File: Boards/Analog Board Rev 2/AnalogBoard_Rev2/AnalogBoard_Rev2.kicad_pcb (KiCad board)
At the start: 4 copper layers, 59.5 x 114.5 mm, 56 parts, among them J1 Conn_01x06_Male, J2 Conn_01x10_Male, J3 Conn_01x06_Male, J4 Conn_01x08_Male, SW1 SW_DIP_x04, U1 OPA2134, U12 NSL-32, U13 NSL-32, U2 OPA2134, U3 OPA2134, U4 OPA2134, U5 OPA2134, U6 NSL-32, U7 NSL-32, U8 NSL-32, U9 NSL-32

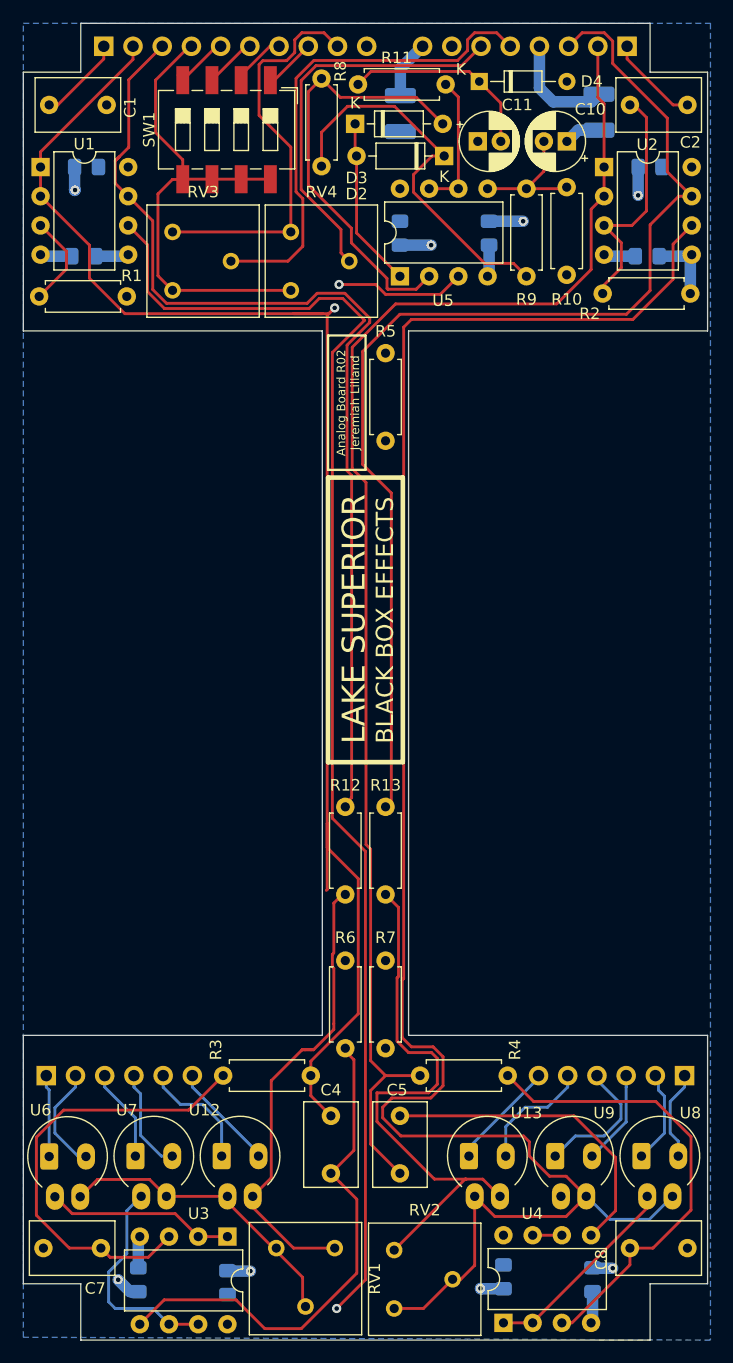
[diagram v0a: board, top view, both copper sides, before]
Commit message: reorg pt 1
Reorganizing, deleted a bunch of stuff. Probably will reorg some more
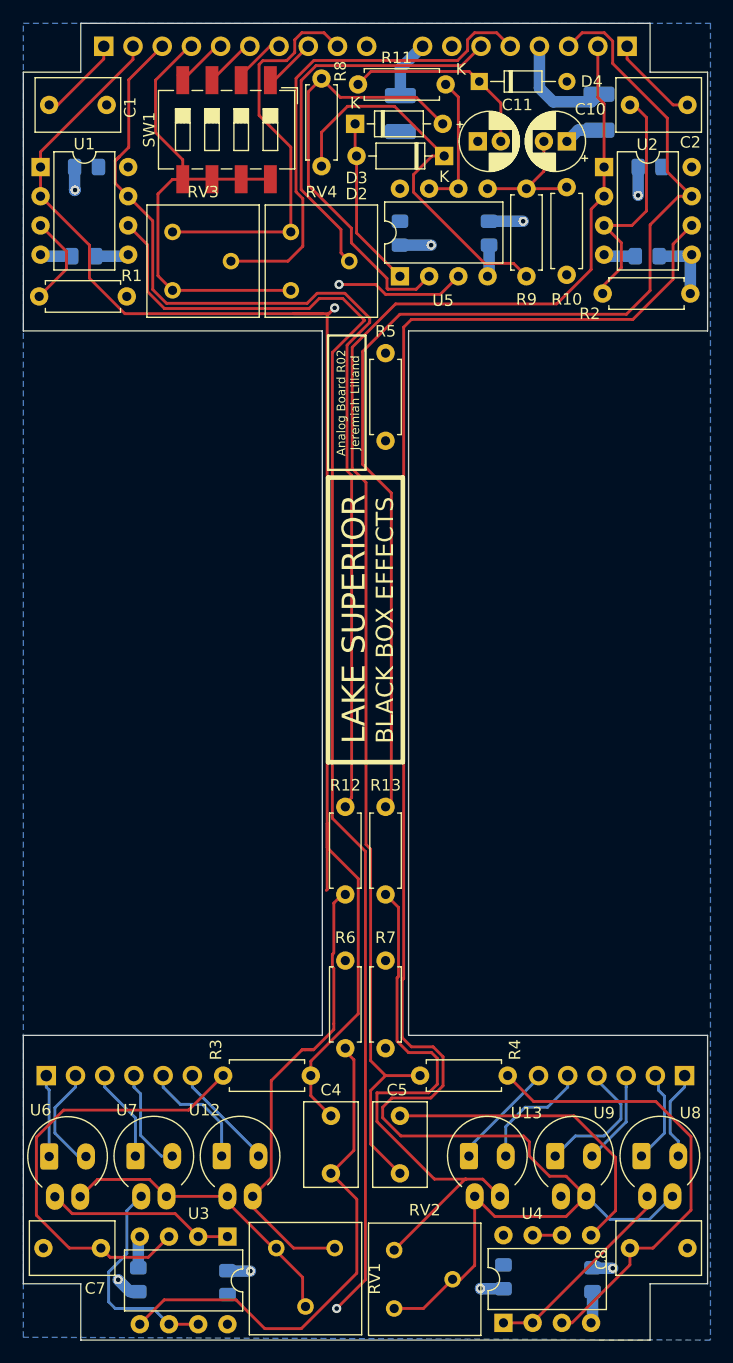
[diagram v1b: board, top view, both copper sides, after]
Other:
- net class Default removed
